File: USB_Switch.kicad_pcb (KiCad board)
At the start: 2 copper layers, 53.3 x 25.4 mm, 18 parts, among them U1 AMS1117-3.3, U2 INA219AxD, U3 INA219AxD, U4 ESP-12F

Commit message: Did work on schematic
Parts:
- added C5: 10uF, Capacitor_SMD:C_0603_1608Metric, F.Cu at (45.1, 86.0)
- added C6: 10uF, Capacitor_SMD:C_0603_1608Metric, F.Cu at (45.1, 89.0)
- added D1: GREEN, LED_SMD:LED_0805_2012Metric, F.Cu at (42.2, 138.7)
- added D2: GREEN, LED_SMD:LED_0805_2012Metric, F.Cu at (42.3, 134.9)
- added J1: Conn_01x06, Connector_PinHeader_2.54mm:PinHeader_1x06_P2.54mm_Vertical, F.Cu at (76.4, 98.7)
- added J2: USB_IN, Library:U217-041N-4BV81, F.Cu at (54.0, 80.3)
- added J3: USB_OUT, Library:904-131A2032S10100, F.Cu at (44.8, 102.1)
- added J4: Conn_01x06, Connector_PinHeader_2.54mm:PinHeader_1x06_P2.54mm_Vertical, F.Cu at (76.5, 129.6)
- added J5: USB_OUT, Library:904-131A2032S10100, F.Cu at (64.5, 102.1)
- added Q1: Q_NMOS_GDS, Library:YJL3400A, F.Cu at (52.0, 93.5)
- added Q2: Q_NMOS_GDS, Library:YJL3400A, F.Cu at (71.7, 93.6)
- added SW1: PRGM, Library:TS-1187A-B-A-B, F.Cu at (67.1, 129.1)
- C1, C2, C3, C4: footprint Capacitor_SMD:C_0402_1005Metric -> Capacitor_SMD:C_0603_1608Metric
- R1, R2: footprint Resistor_SMD:R_0402_1005Metric -> Resistor_SMD:R_2010_5025Metric
- R10, R3, R4, R5, R6, R7, R8, R9: footprint Resistor_SMD:R_0402_1005Metric -> Resistor_SMD:R_0603_1608Metric
- moved R9 68.6 mm to (44.8, 133.8), turned to 0 degrees
- moved C4 57.4 mm to (44.0, 140.6), turned to -90 degrees
- moved R10 57.3 mm to (66.1, 135.8), turned to 180 degrees
- moved C3 57.3 mm to (45.6, 140.6), turned to -90 degrees
- moved R7 56.6 mm to (44.8, 137.8)
- moved R4 56.4 mm to (44.8, 129.8)
- moved R8 56.4 mm to (44.8, 135.8)
- moved R3 56.4 mm to (44.8, 125.8)
- moved U4 56.2 mm to (55.4, 129.3)
- moved R6 55.7 mm to (65.3, 138.8)
- moved R5 54.4 mm to (66.1, 133.8), turned to 0 degrees
- moved R2 49.0 mm to (70.3, 97.0), turned to 180 degrees
- moved C2 40.5 mm to (66.3, 97.1), turned to 90 degrees
- moved U1 40.4 mm to (39.9, 87.5), turned to 180 degrees
- moved R1 39.7 mm to (50.6, 96.9), turned to 180 degrees
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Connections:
- net /Control Board/C_GND renamed GND
- net /Control Board/LED_OFF renamed /Control Board/LED_2
- net /Control Board/LED_ON renamed /Control Board/LED_1
- C1 pad 1: /Control Board/C_3v3 -> /MOSFET Board/M_3v3
- C2 pad 1: /Control Board/C_3v3 -> /MOSFET Board/M_3v3
- R1 pad 2: /MOSFET Board/5V_OUT -> /MOSFET Board/5V_OUT_1
- R2 pad 2: /MOSFET Board/5V_OUT -> /MOSFET Board/5V_OUT_2
- U1 pad 2: /Control Board/C_3v3 -> /MOSFET Board/M_3v3
- U2 pad 3: /Control Board/C_I2C_SDA -> /MOSFET Board/M_I2C_SDA
- U2 pad 4: /Control Board/C_I2C_SCL -> /MOSFET Board/M_I2C_SCL
- U2 pad 5: /Control Board/C_3v3 -> /MOSFET Board/M_3v3
- U2 pad 7: /MOSFET Board/5V_OUT -> /MOSFET Board/5V_OUT_1
- U3 pad 2: /Control Board/C_3v3 -> /MOSFET Board/M_3v3
- U3 pad 3: /Control Board/C_I2C_SDA -> /MOSFET Board/M_I2C_SDA
- U3 pad 4: /Control Board/C_I2C_SCL -> /MOSFET Board/M_I2C_SCL
- U3 pad 5: /Control Board/C_3v3 -> /MOSFET Board/M_3v3
- U3 pad 7: /MOSFET Board/5V_OUT -> /MOSFET Board/5V_OUT_2
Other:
- board size 53.3 x 25.4 mm -> 43.3 x 61.8 mm
- board text added: "V-CUT"

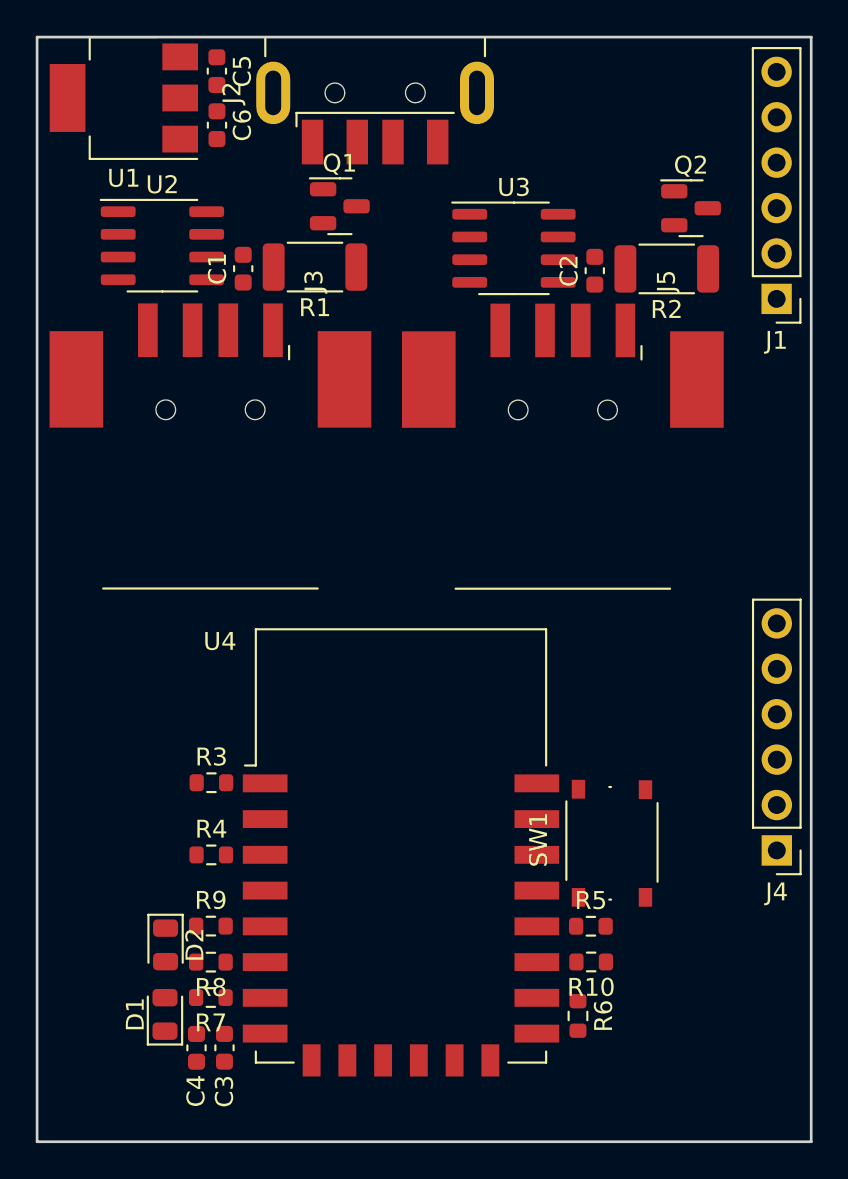
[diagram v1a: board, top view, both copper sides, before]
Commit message: Finished initial layout of PCB
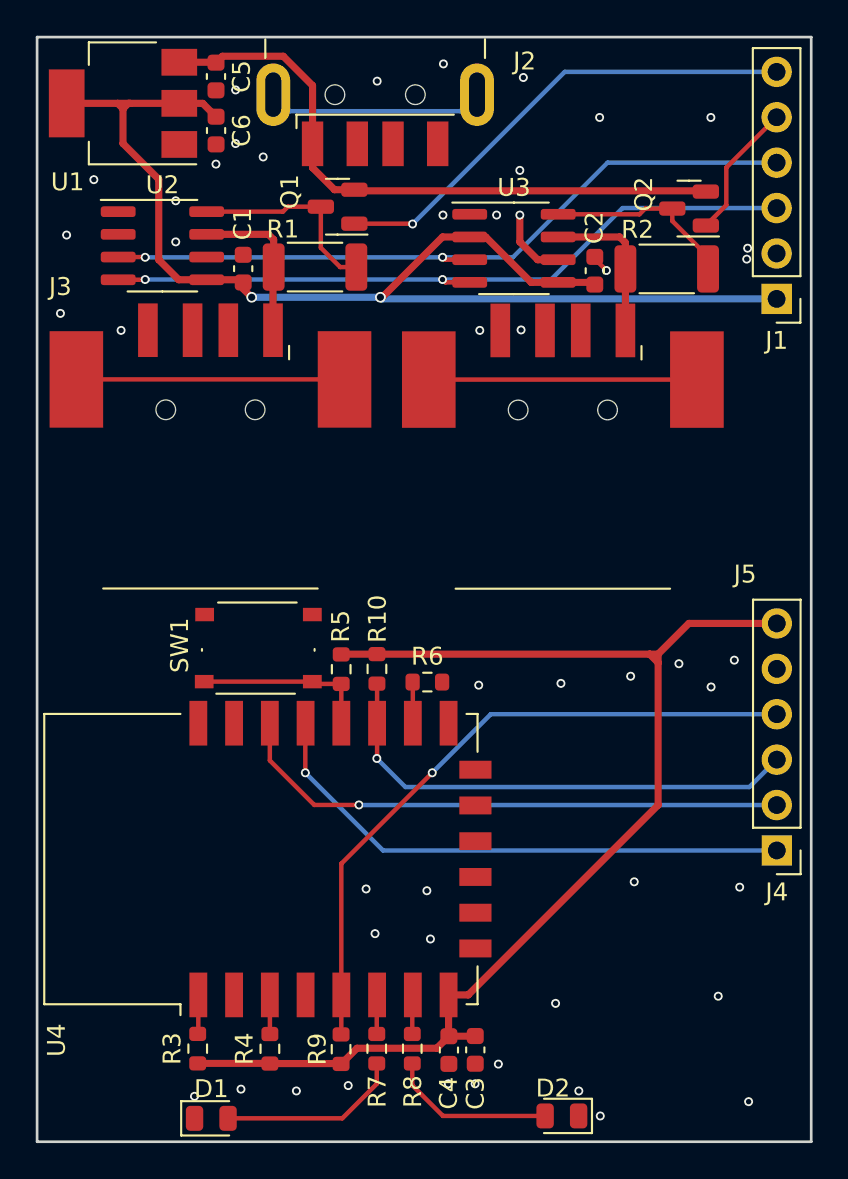
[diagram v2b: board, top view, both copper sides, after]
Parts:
- moved D2 24.1 mm to (64.4, 144.4), turned to 180 degrees
- moved SW1 22.5 mm to (47.4, 118.4), turned to 180 degrees
- moved R6 20.5 mm to (56.9, 120.2), turned to 180 degrees
- moved R10 20.3 mm to (54.1, 119.4), turned to -90 degrees
- moved R5 20.0 mm to (52.1, 119.4), turned to 90 degrees
- moved R3 14.9 mm to (44.1, 140.7), turned to 90 degrees
- moved C4 14.1 mm to (58.1, 140.7)
- moved C3 14.0 mm to (59.6, 140.7)
- moved R8 12.3 mm to (56.1, 140.7), turned to -90 degrees
- moved R4 11.3 mm to (48.1, 140.7), turned to 90 degrees
- moved R9 10.0 mm to (52.1, 140.7), turned to 90 degrees
- moved R7 9.71 mm to (54.1, 140.7), turned to -90 degrees
- moved U4 7.87 mm to (47.6, 130.1), turned to 90 degrees
- moved D1 6.37 mm to (44.8, 144.6), turned to 0 degrees
- moved U1 0.30 mm to (39.9, 87.8)
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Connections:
- U4 pad 6: /Control Board/LED_2 -> /Control Board/LED_1
- U4 pad 7: /Control Board/LED_1 -> /Control Board/LED_2
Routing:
- net /MOSFET Board/M_3v3: track 0.00 -> 69.1 mm, vias 0 -> 2
- net /Control Board/C_3v3: track 0.00 -> 68.8 mm
- net /MOSFET Board/M_I2C_SDA: track 0.00 -> 40.6 mm, vias 0 -> 2
- net /MOSFET Board/M_I2C_SCL: track 0.00 -> 40.1 mm, vias 0 -> 2
- net /Control Board/C_I2C_SCL: track 0.00 -> 37.4 mm, vias 0 -> 1
- net /MOSFET Board/5V_IN: track 0.00 -> 35.4 mm
- net /Control Board/M2_TOGGLE: track 0.00 -> 31.5 mm, vias 0 -> 1
- net /Control Board/M1_TOGGLE: track 0.00 -> 31.0 mm, vias 0 -> 1
- net /Control Board/C_I2C_SDA: track 0.00 -> 27.9 mm, vias 0 -> 1
- net /MOSFET Board/M1_TOGGLE: track 0.00 -> 27.2 mm, vias 0 -> 1
- net unconnected-(J5-Pad5): track 0.00 -> 15.0 mm
- net unconnected-(J3-Pad5): track 0.00 -> 15.0 mm
- net unconnected-(J2-Pad5): track 0.00 -> 12.2 mm
- net Net-(Q1-Pad3): track 0.00 -> 11.2 mm
- net Net-(Q2-Pad3): track 0.00 -> 10.7 mm
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- added copper zone on B.Cu, net GND
- added copper zone on F.Cu, net GND

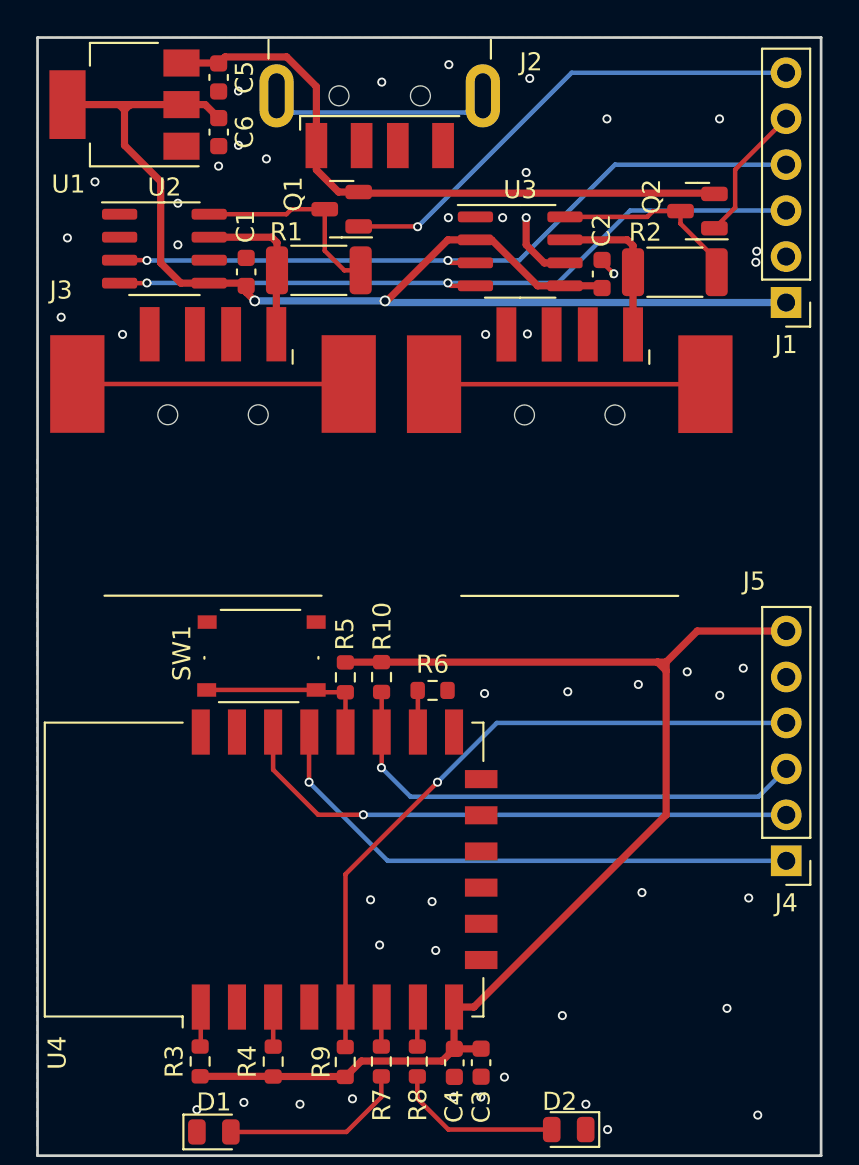
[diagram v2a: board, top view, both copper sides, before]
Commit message: Added TX/RX to schematic. Updated PCB
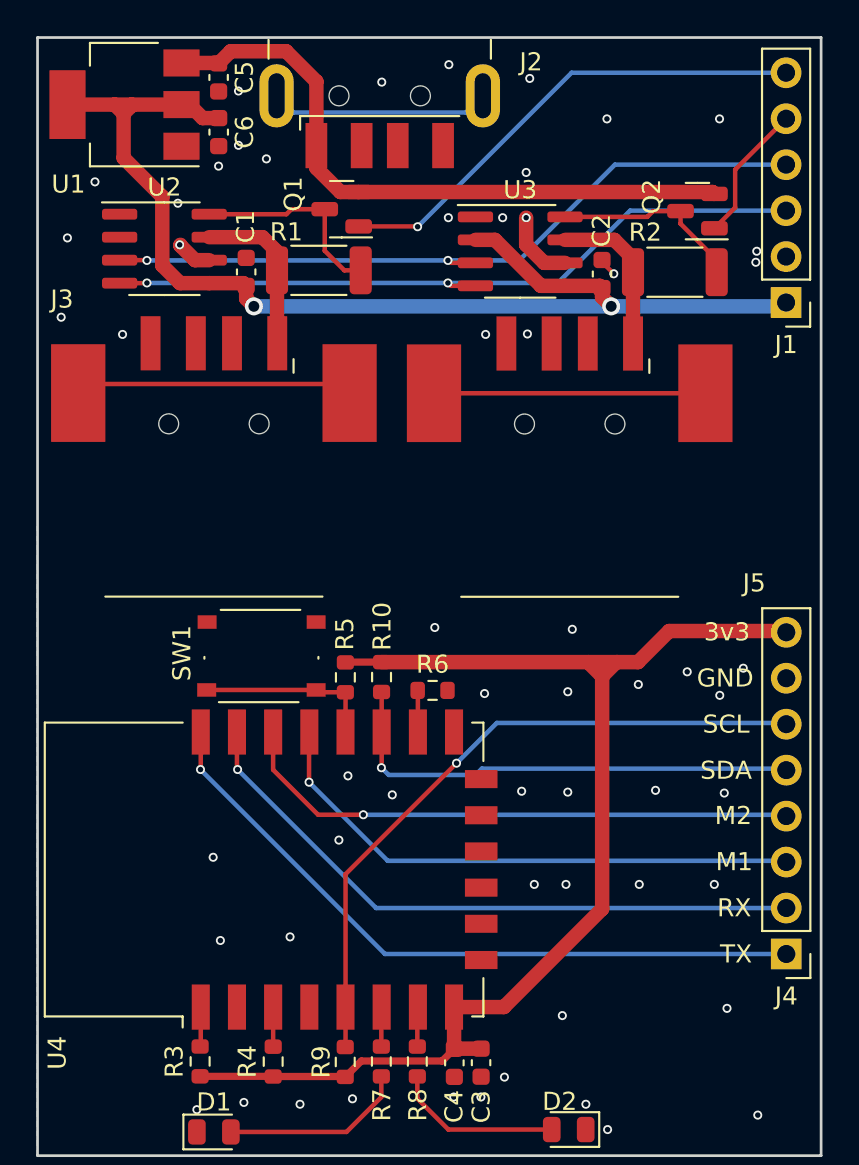
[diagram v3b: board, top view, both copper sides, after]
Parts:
- J4: value Conn_01x06 -> Conn_01x08; footprint Connector_PinHeader_2.54mm:PinHeader_1x06_P2.54mm_Vertical -> Connector_PinHeader_2.54mm:PinHeader_1x08_P2.54mm_Vertical
- moved J4 5.15 mm to (76.5, 134.7)
- moved J3 0.50 mm to (44.8, 102.6)
- moved J5 0.50 mm to (64.5, 102.6)
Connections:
- J4 pad 1: /Control Board/M1_TOGGLE -> /Control Board/C_TX
- J4 pad 2: /Control Board/M2_TOGGLE -> /Control Board/C_RX
- J4 pad 3: /Control Board/C_I2C_SDA -> /Control Board/M1_TOGGLE
- J4 pad 4: /Control Board/C_I2C_SCL -> /Control Board/M2_TOGGLE
- J4 pad 5: GND -> /Control Board/C_I2C_SDA
- J4 pad 6: /Control Board/C_3v3 -> /Control Board/C_I2C_SCL
- U4 pad 21: unconnected-(U4-Pad21) -> /Control Board/C_RX
- U4 pad 22: unconnected-(U4-Pad22) -> /Control Board/C_TX
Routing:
- net /Control Board/C_TX: track 0.00 -> 38.7 mm, vias 0 -> 1
- net /Control Board/C_RX: track 0.00 -> 35.6 mm, vias 0 -> 1
- net /MOSFET Board/M_3v3: track 69.1 -> 64.6 mm
- net GND: track 5.09 -> 7.06 mm, vias 48 -> 58
- net /Control Board/C_I2C_SDA: track 27.9 -> 26.9 mm
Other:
- board text added: "3v3"
- board text added: "GND"
- board text added: "M1"
- board text added: "M2"
- board text added: "RX"
- board text added: "SCL"
- board text added: "SDA"
- board text added: "TX"

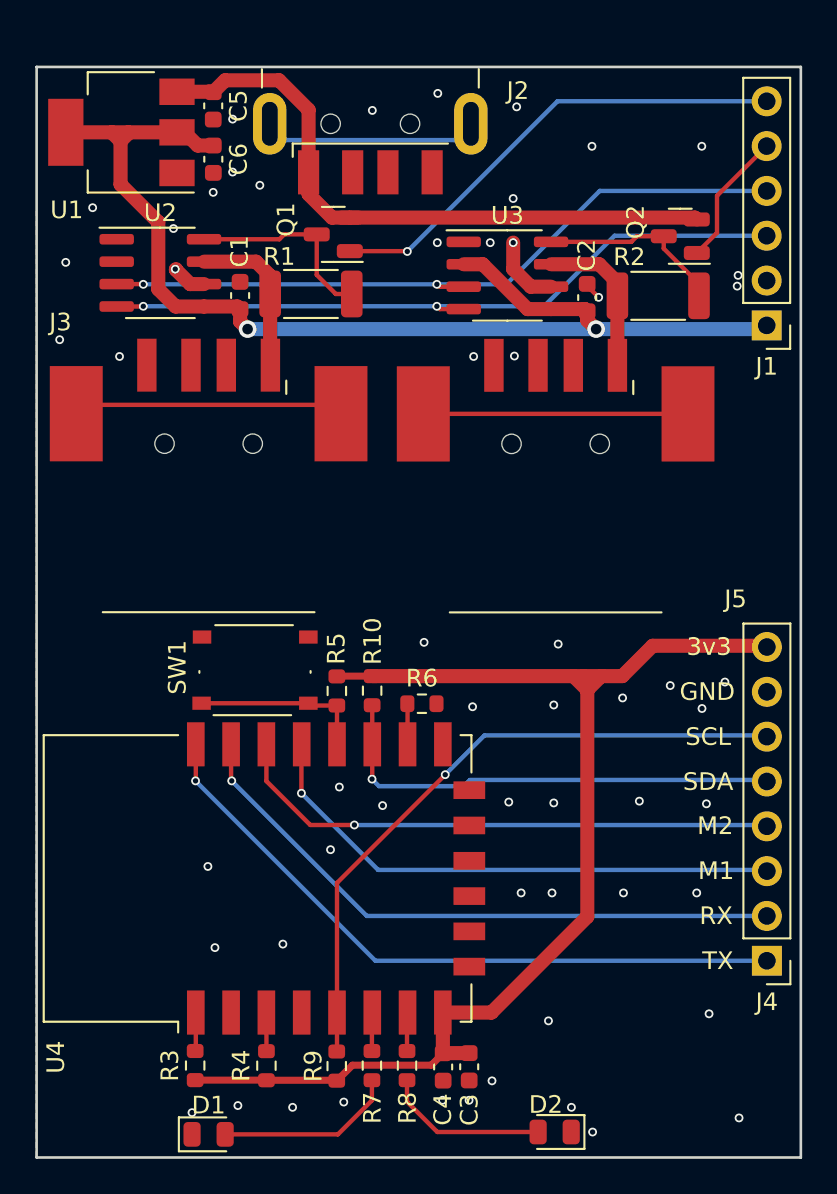
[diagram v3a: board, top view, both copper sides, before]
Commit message: Updated PCB layout to have cleaner dimensions
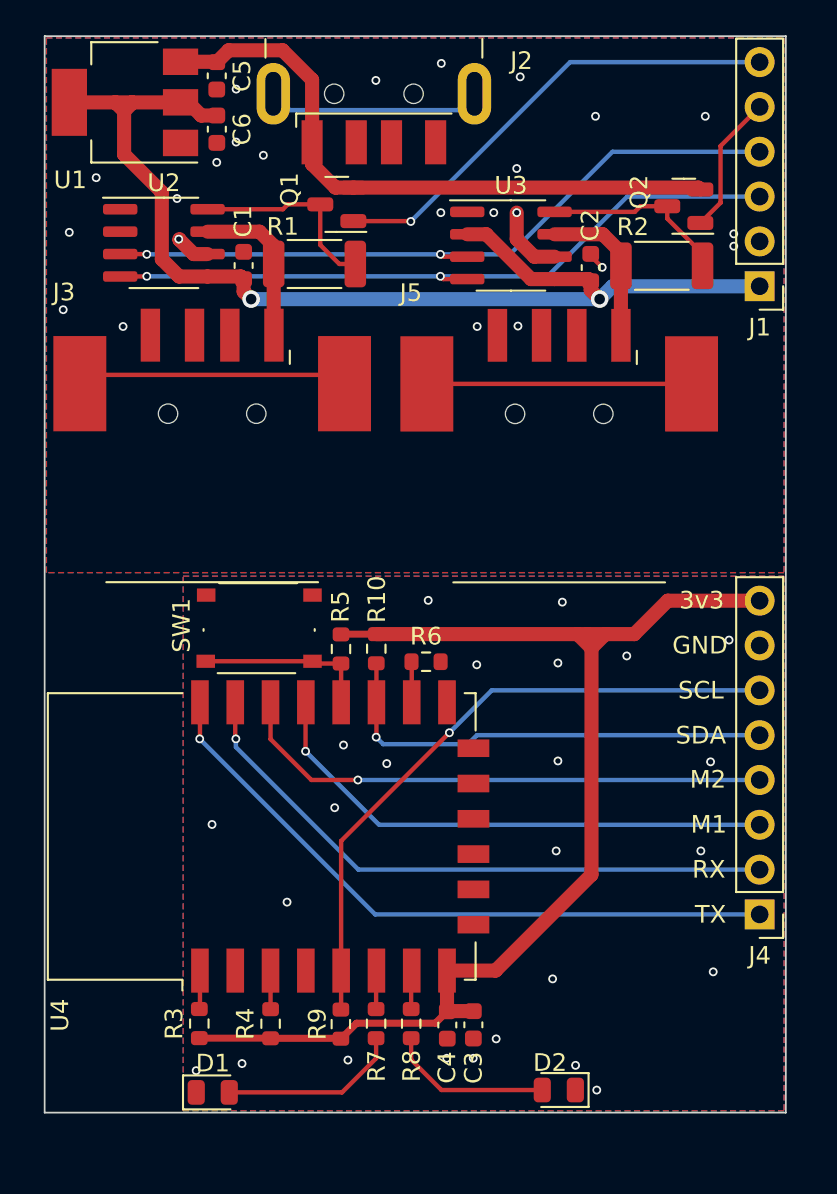
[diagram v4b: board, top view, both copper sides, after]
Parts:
- moved J4 2.66 mm to (76.0, 132.1)
- moved D2 2.39 mm to (64.7, 142.0)
- moved C3 2.39 mm to (59.8, 138.4)
- moved C4 2.39 mm to (58.3, 138.4)
- moved D1 2.39 mm to (45.1, 142.2)
- moved R10 2.39 mm to (54.3, 117.0)
- moved R3 2.39 mm to (44.3, 138.3)
- moved R4 2.39 mm to (48.3, 138.3)
- moved R5 2.39 mm to (52.3, 117.1)
- moved R6 2.39 mm to (57.1, 117.8)
- moved R7 2.39 mm to (54.3, 138.3)
- moved R8 2.39 mm to (56.3, 138.3)
- moved R9 2.39 mm to (52.3, 138.3)
- moved SW1 2.39 mm to (47.6, 116.0)
- moved U4 2.39 mm to (47.8, 127.7)
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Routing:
- net /Control Board/C_TX: track 38.7 -> 37.9 mm
- net /Control Board/M1_TOGGLE: track 31.0 -> 30.2 mm
- net /Control Board/M2_TOGGLE: track 31.5 -> 30.8 mm
- net /Control Board/C_I2C_SDA: track 26.9 -> 26.3 mm
- net /Control Board/C_3v3: track 69.2 -> 68.6 mm
- net /Control Board/C_I2C_SCL: track 37.4 -> 36.8 mm
- net GND: vias 58 -> 49
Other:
- board size 43.3 x 61.8 mm -> 42 x 61 mm
- board text added: "V-SCORE"
- board text removed: "V-CUT"
